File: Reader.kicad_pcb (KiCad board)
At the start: 2 copper layers, 40.4 x 60 mm, 41 parts, among them J1 Conn_01x04, J2 Amphenol Dubox ‎76383-402LF‎, J3 Conn_01x04, J4 Conn_01x08, J5 Conn_01x10, J6 Conn_01x03, J7 Conn_01x02, Q1 2N7002, Q2 2N7002, Q3 2N7002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

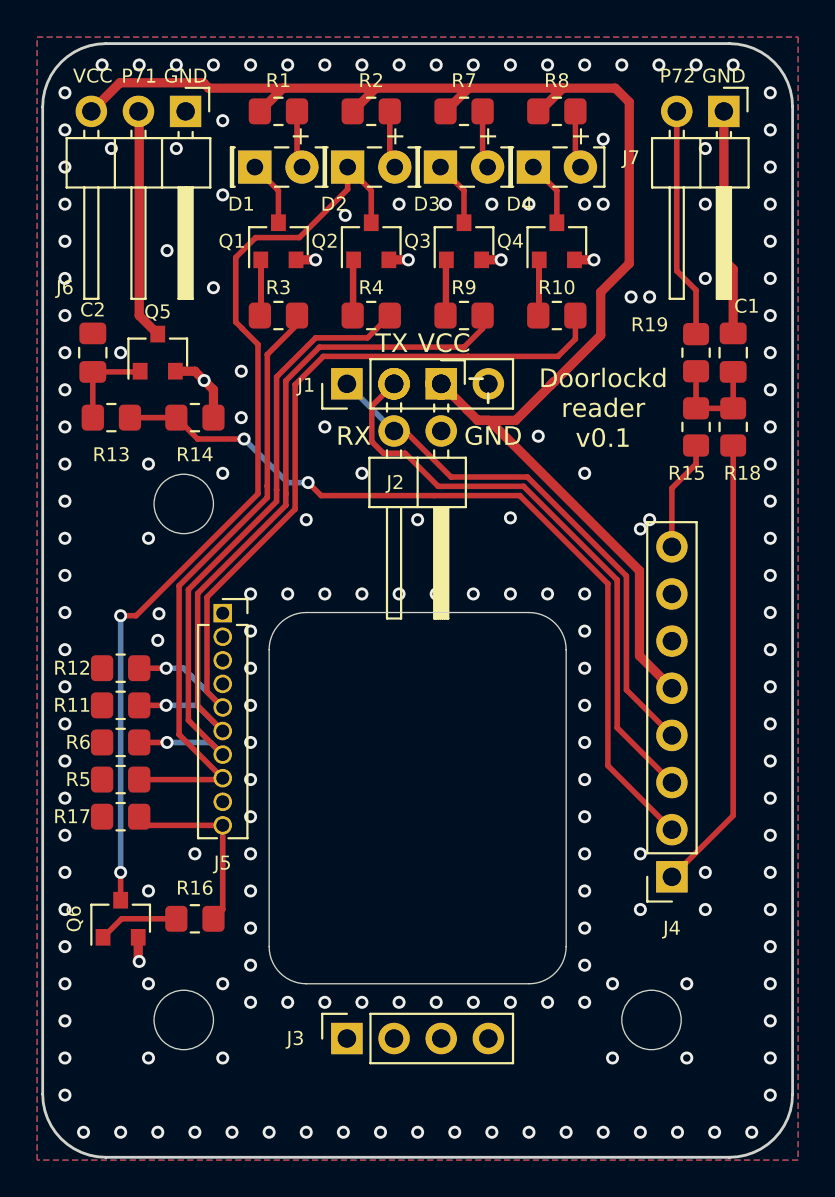
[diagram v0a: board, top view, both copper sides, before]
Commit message: Reduce overly wide thermal reliefs due to wide GND traces
The thermal relief spoke width was 0,3mm, but there were also explicit
GND traces of 0,5mm that made some components (esp C1 and some
transistors) hard to solder. This reduces the trace width to 0,3mm,
hopefully alleviating this issue.
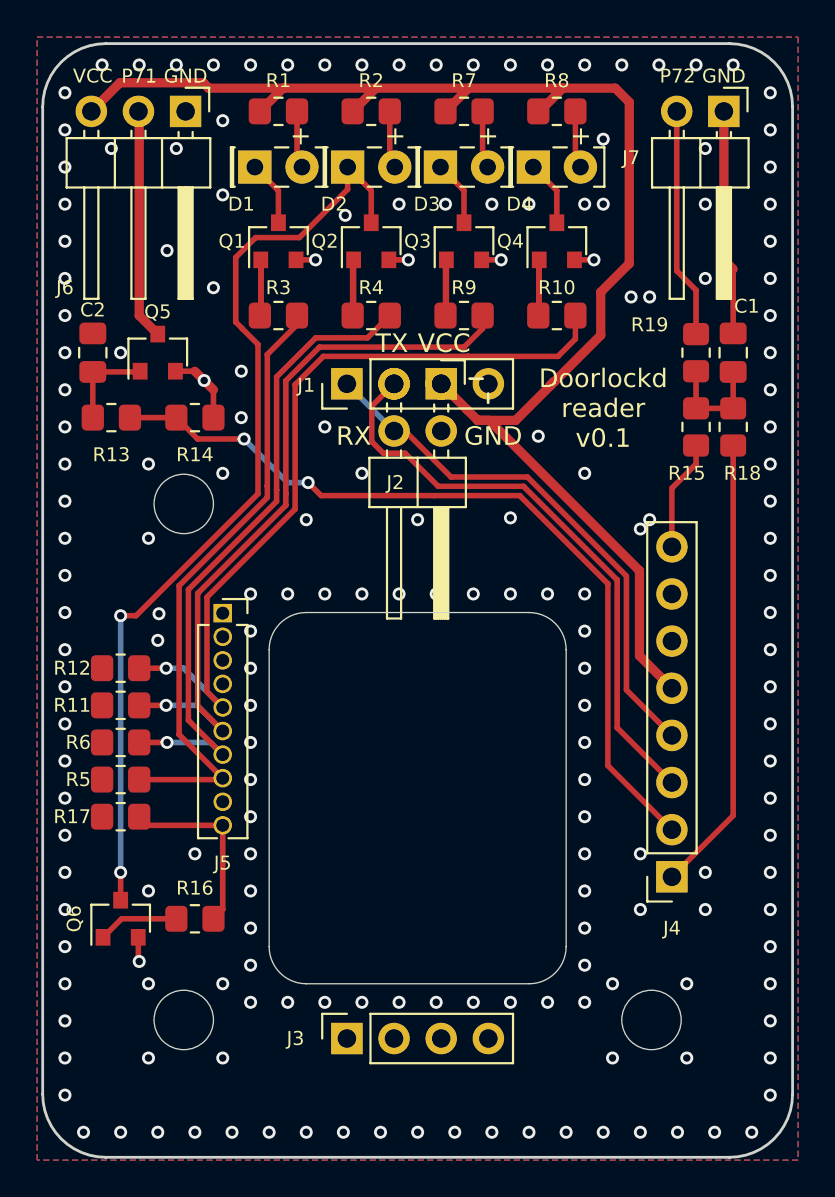
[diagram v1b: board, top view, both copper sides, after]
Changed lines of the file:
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@@
     (style (thickness 0.15) (arrow_length 1.27) (text_position_mode 0) (extension_height 0.58642) (extension_offset 0) keep_text_aligned)
   )
-  (segment (start 89 80) (end 89 81.5) (width 0.5) (layer "F.Cu") (net 1))
+  (segment (start 89 80) (end 89 81.5) (width 0.3) (layer "F.Cu") (net 1))
   (segment (start 88 79) (end 88.5 79.5) (width 0.5) (layer "F.Cu") (net 1))
   (segment (start 88.5 79.5) (end 89 80) (width 0.5) (layer "F.Cu") (net 1))
-  (segment (start 86.95 79) (end 88 79) (width 0.5) (layer "F.Cu") (net 1))
-  (segment (start 84.95 109.5) (end 84.95 110.75) (width 0.5) (layer "F.Cu") (net 1))
+  (segment (start 86.95 79) (end 88 79) (width 0.3) (layer "F.Cu") (net 1))
+  (segment (start 84.95 109.5) (end 84.95 110.75) (width 0.3) (layer "F.Cu") (net 1))
   (segment (start 84.95 110.75) (end 85 110.8) (width 0.5) (layer "F.Cu") (net 1))
   (segment (start 98.45 73) (end 98.5 73) (width 0.5) (layer "F.Cu") (net 1))
   (segment (start 116.5 73) (end 117 73.5) (width 0.5) (layer "F.Cu") (net 1))
-  (segment (start 117 73.5) (end 117 76.9625) (width 0.5) (layer "F.Cu") (net 1))
-  (segment (start 93.45 73) (end 94.5 73) (width 0.5) (layer "F.Cu") (net 1))
-  (segment (start 98.5 73) (end 99.5 73) (width 0.5) (layer "F.Cu") (net 1))
+  (segment (start 117 73.5) (end 117 76.9625) (width 0.3) (layer "F.Cu") (net 1))
+  (segment (start 93.45 73) (end 94.5 73) (width 0.3) (layer "F.Cu") (net 1))
+  (segment (start 98.5 73) (end 99.5 73) (width 0.3) (layer "F.Cu") (net 1))
   (segment (start 116.5 65) (end 116.5 73) (width 0.5) (layer "F.Cu") (net 1))
-  (segment (start 108.45 73) (end 109.5 73) (width 0.5) (layer "F.Cu") (net 1))
-  (segment (start 103.45 73) (end 104.5 73) (width 0.5) (layer "F.Cu") (net 1))
+  (segment (start 108.45 73) (end 109.5 73) (width 0.3) (layer "F.Cu") (net 1))
+  (segment (start 103.45 73) (end 104.5 73) (width 0.3) (layer "F.Cu") (net 1))
   (via (at 81 94) (size 0.7) (drill 0.4) (layers "F.Cu" "B.Cu") (net 1))
   (via (at 91 111) (size 0.7) (drill 0.4) (layers "F.Cu" "B.Cu") (net 1))

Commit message: Add input supply buffer cap
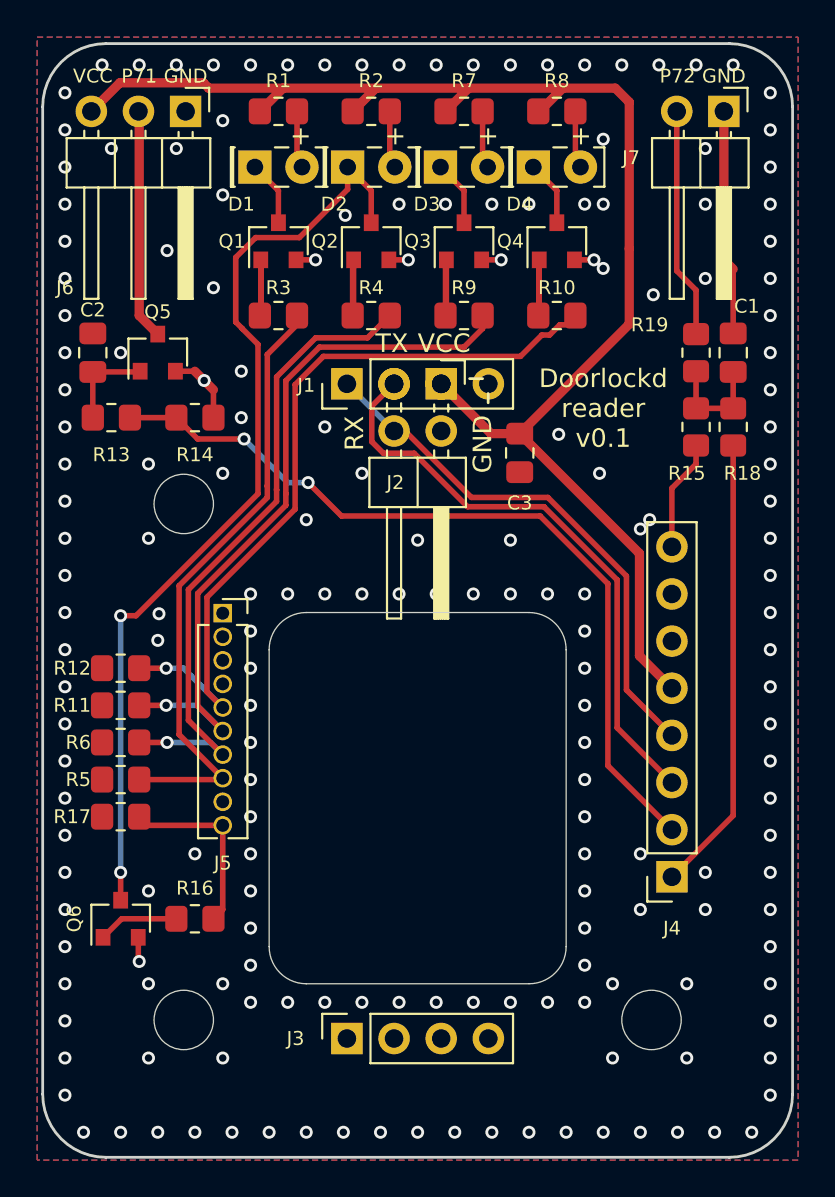
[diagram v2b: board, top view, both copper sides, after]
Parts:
- added C3: 10uF, Capacitor_SMD:C_0805_2012Metric_Pad1.18x1.45mm_HandSolder, F.Cu at (105.5, 83.4)
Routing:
- net VCC: track 81.2 -> 79.9 mm

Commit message: Use hand soldering footprints for transistors
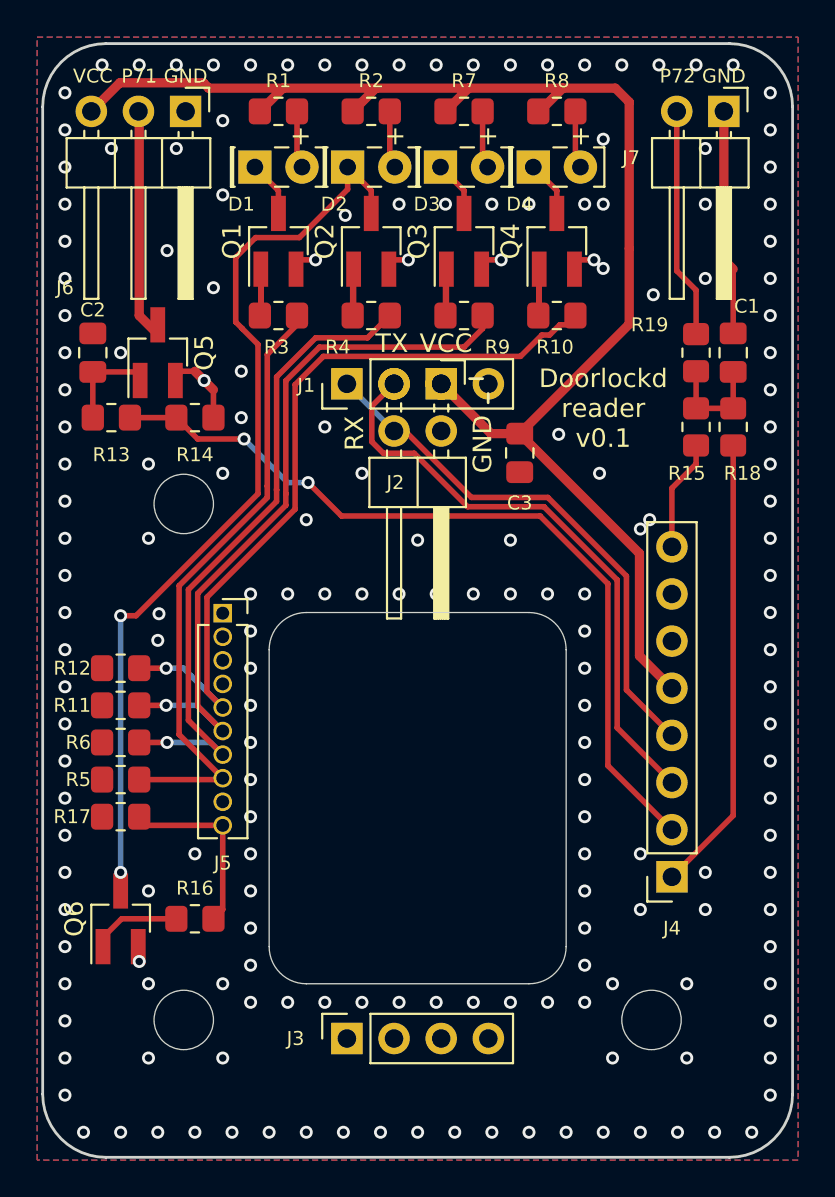
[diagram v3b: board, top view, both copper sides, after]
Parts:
- Q1, Q2, Q3, Q4, Q5, Q6: footprint Package_TO_SOT_SMD:SOT-23 -> Package_TO_SOT_SMD:SOT-23_Handsoldering
